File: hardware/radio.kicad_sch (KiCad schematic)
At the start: 0 parts

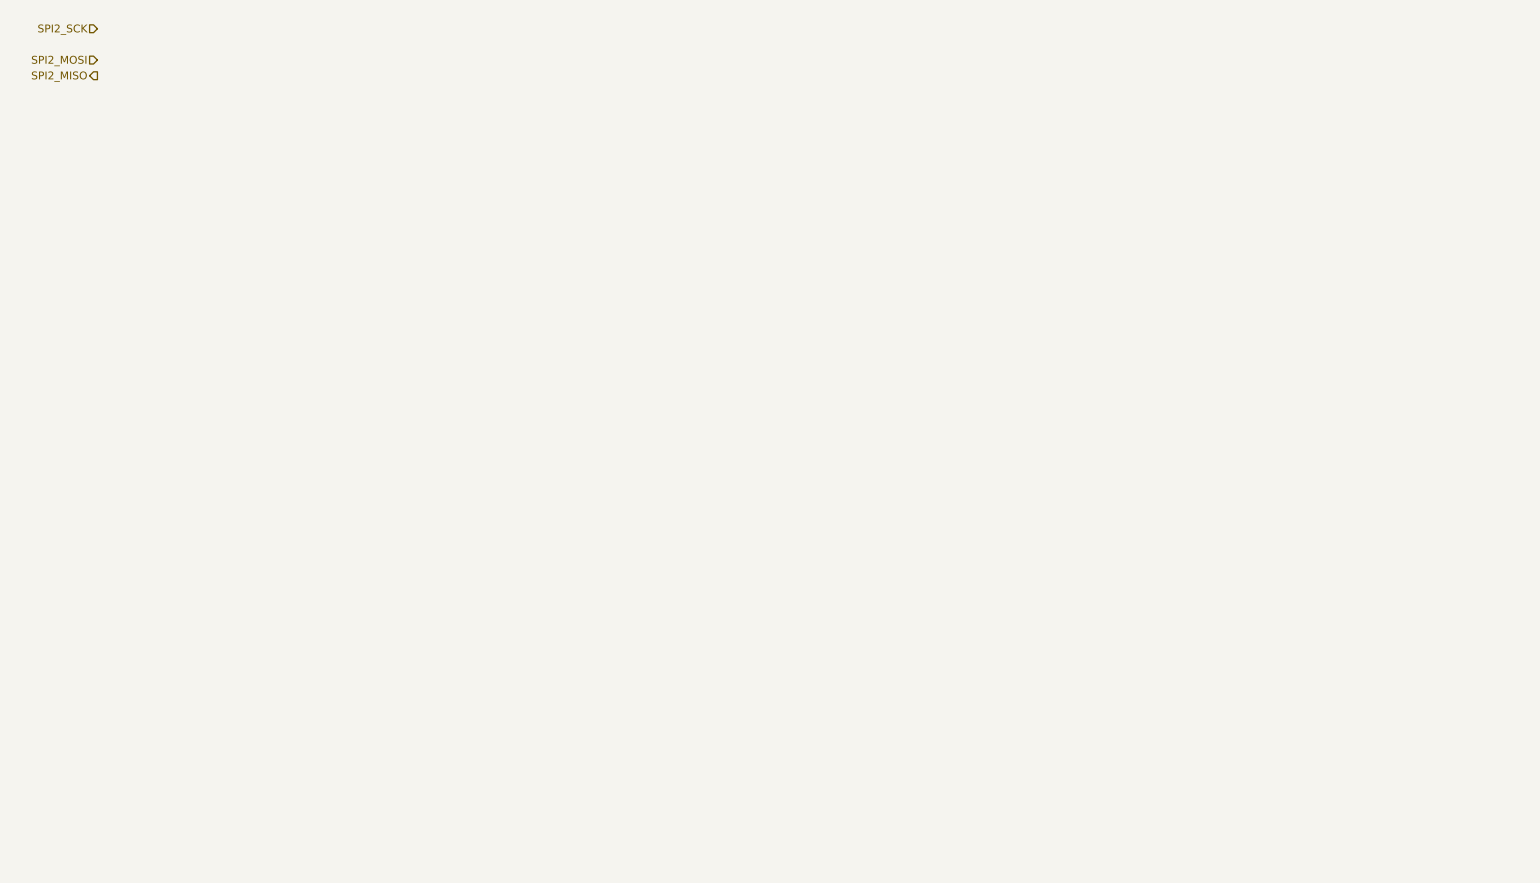
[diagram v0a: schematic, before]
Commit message: feat(kicad): Added several open sourced footprint libraries, finished schematic design for nrf, uwb, tof, flash, motors and added all reference material to refs folder
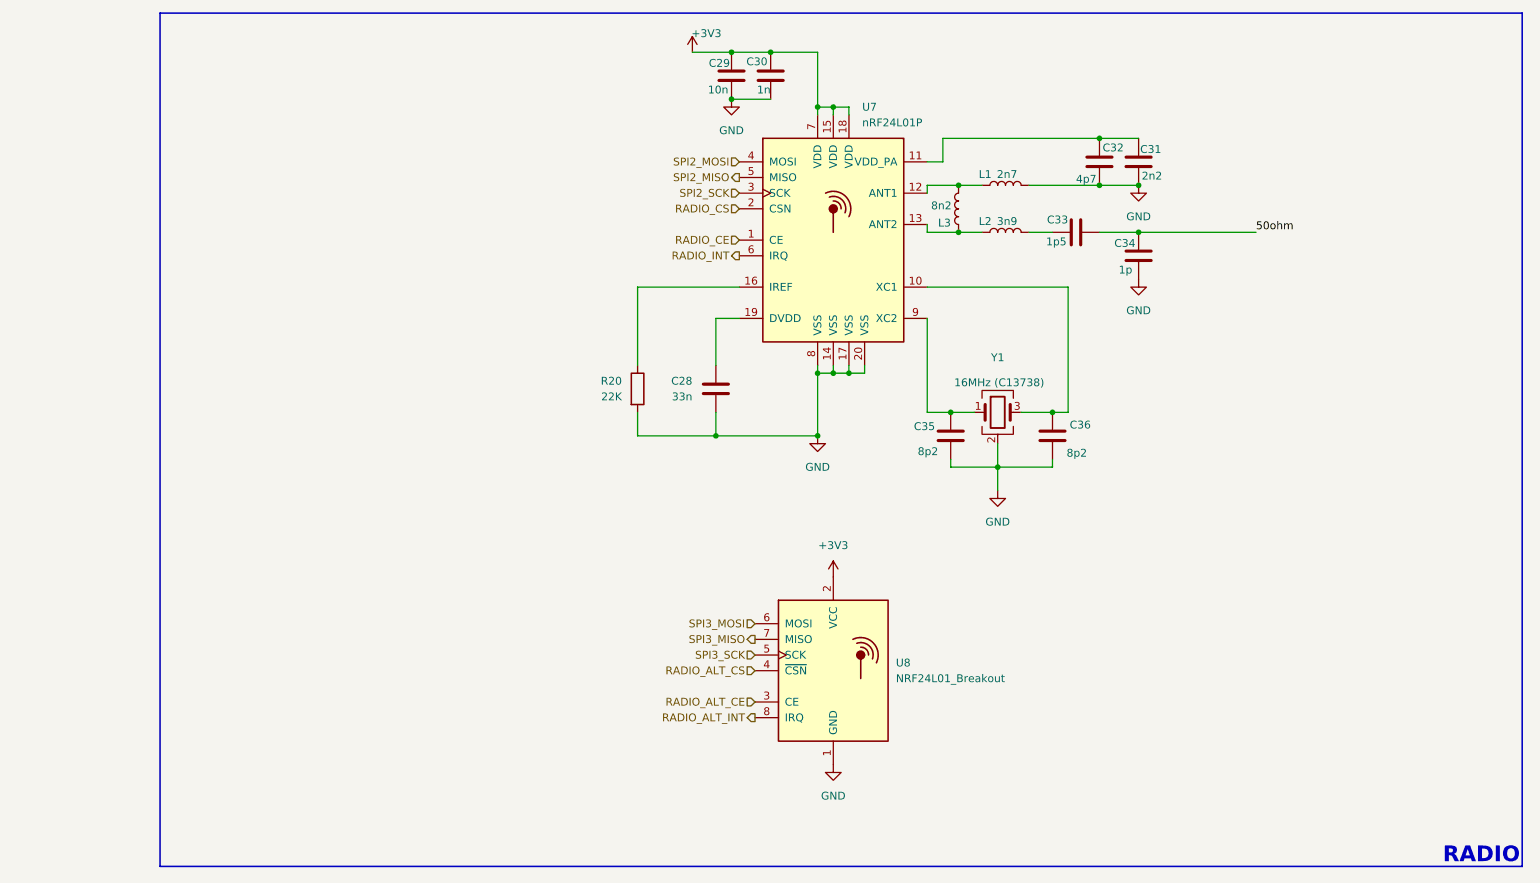
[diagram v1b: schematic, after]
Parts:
- added C28: 33n, symbol Device:C
- added C29: 10n, symbol Device:C
- added C30: 1n, symbol Device:C
- added C31: 2n2, symbol Device:C
- added C32: 4p7, symbol Device:C
- added C33: 1p5, symbol Device:C
- added C34: 1p, symbol Device:C
- added C35, C36: 8p2, symbol Device:C
- added L1: 2n7, symbol Device:L
- added L2: 3n9, symbol Device:L
- added L3: 8n2, symbol Device:L
- added R20: 22K, symbol Device:R
- added U7: nRF24L01P, Package_DFN_QFN:QFN-20-1EP_4x4mm_P0.5mm_EP2.5x2.5mm, symbol RF:nRF24L01P
- added U8: NRF24L01_Breakout, RF_Module:nRF24L01_Breakout, symbol RF:NRF24L01_Breakout
- added Y1: 16MHz (C13738), symbol Device:Crystal_GND24
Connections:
- net SPI2_MISO: now also U7.5 (MISO)
- net SPI2_MOSI: now also U7.4 (MOSI)
- net SPI2_SCK: now also U7.3 (SCK)
- new net: C31.1, C32.1, U7.11 (VDD_PA)
- new net: L1.1, L3.2, U7.12 (ANT1)
- new net: R20.1, U7.16 (IREF)
- new net: C33.1, L2.2
- new net: C35.1, U7.9 (XC2), Y1.1
- new net: C36.1, U7.10 (XC1), Y1.3
- new net: L2.1, L3.1, U7.13 (ANT2)
- new net: C28.1, U7.19 (DVDD)
- new net +3V3: C29.1, C30.1, U7.15 (VDD), U7.18 (VDD), U7.7 (VDD), U8.2 (VCC)
- new net 50ohm: C33.2, C34.2
- new net GND: C28.2, C29.2, C30.2, C31.2, C32.2, C34.1, C35.2, C36.2, L1.2, R20.2, U7.14 (VSS), U7.17 (VSS), U7.20 (VSS), U7.8 (VSS), U8.1 (GND), Y1.2 (G), Y1.4 (G)
- new net RADIO_ALT_CE: U8.3 (CE)
- new net RADIO_ALT_CS: U8.4 (~{CSN})
- new net RADIO_ALT_INT: U8.8 (IRQ)
- new net RADIO_CE: U7.1 (CE)
- new net RADIO_CS: U7.2 (CSN)
- new net RADIO_INT: U7.6 (IRQ)
- new net SPI3_MISO: U8.7 (MISO)
- new net SPI3_MOSI: U8.6 (MOSI)
- new net SPI3_SCK: U8.5 (SCK)
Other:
- note added: "RADIO"
